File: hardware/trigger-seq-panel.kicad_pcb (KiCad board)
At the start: 2 copper layers, 89.1 x 104.6 mm, 98 parts, among them J1 OUT1, J2 OUT2, J3 RESET, J4 CLOCK_IN, J5 RUN_STOP, J6 UP_DOWN, J7 CLOCK_OUT, P3 SWITCH_PANEL, P8 JACKS_PANEL, Q6 2N3904, SW1 SW_SPDT, SW10 SW_SPDT, SW11 SW_SPDT, SW12 SW_SPDT, SW13 SW_SPDT, SW14 SW_SPDT, SW15 SW_SPDT, SW16 SW_SPDT, SW17 SW_SPDT, SW18 Run/Stop, SW19 Up/Down, SW2 SW_SPDT, SW20 RESET, SW3 SW_SPDT, SW4 SW_SPDT, SW5 SW_SPDT, SW6 SW_SPDT, SW7 SW_SPDT, SW8 SW_SPDT, SW9 SW_DPDT_x2, U2 TL072

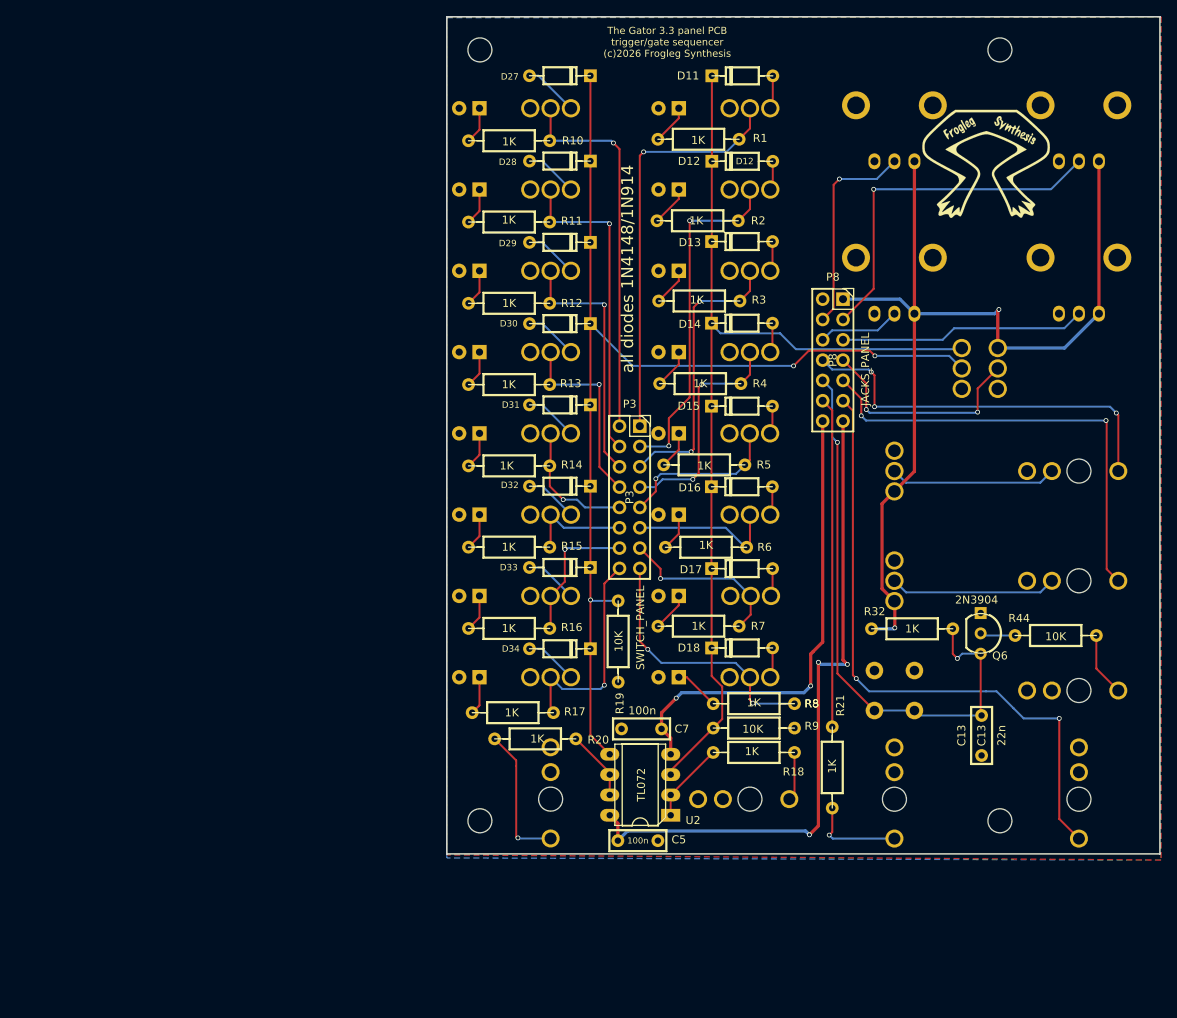
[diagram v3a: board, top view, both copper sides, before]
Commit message: update for version 3.3, slight tweaks to v3.2 which has now passed smoke test.
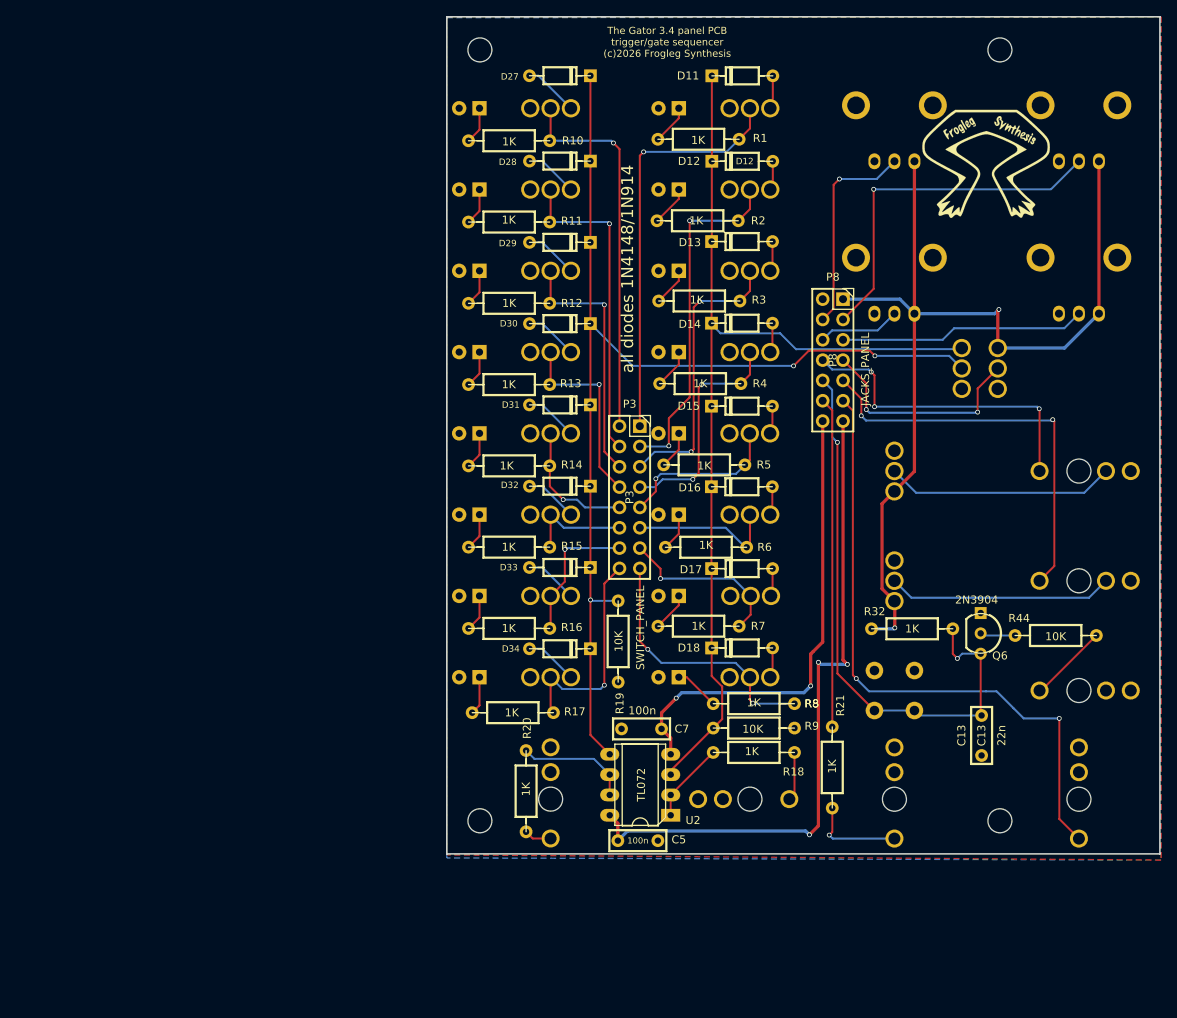
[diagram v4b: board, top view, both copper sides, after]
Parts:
- moved R20 12.3 mm to (129.0, 136.7), turned to 90 degrees
- turned J3 to -90 degrees
- turned J5 to -90 degrees
- turned J6 to -90 degrees
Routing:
- net Net-(J2-Pad1): track 17.8 -> 3.41 mm, vias 1 -> 0
- net R/S: track 49.1 -> 39.7 mm
- net Net-(J5-Pad2): track 20.9 -> 28.7 mm
- net Net-(J6-Pad2): track 20.9 -> 28.2 mm
- net U/D: track 57.1 -> 50.6 mm
- net Net-(R20-Pad2): track 8.76 -> 14.2 mm
- net Net-(J3-Pad1): track 8.01 -> 9.95 mm
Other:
- board text added: "The Gator 3.4 panel PCB trigger/gate sequencer (c)2026 Frogleg Synthesis"
- board text removed: "The Gator 3.3 panel PCB trigger/gate sequencer (c)2026 Frogleg Synthesis"

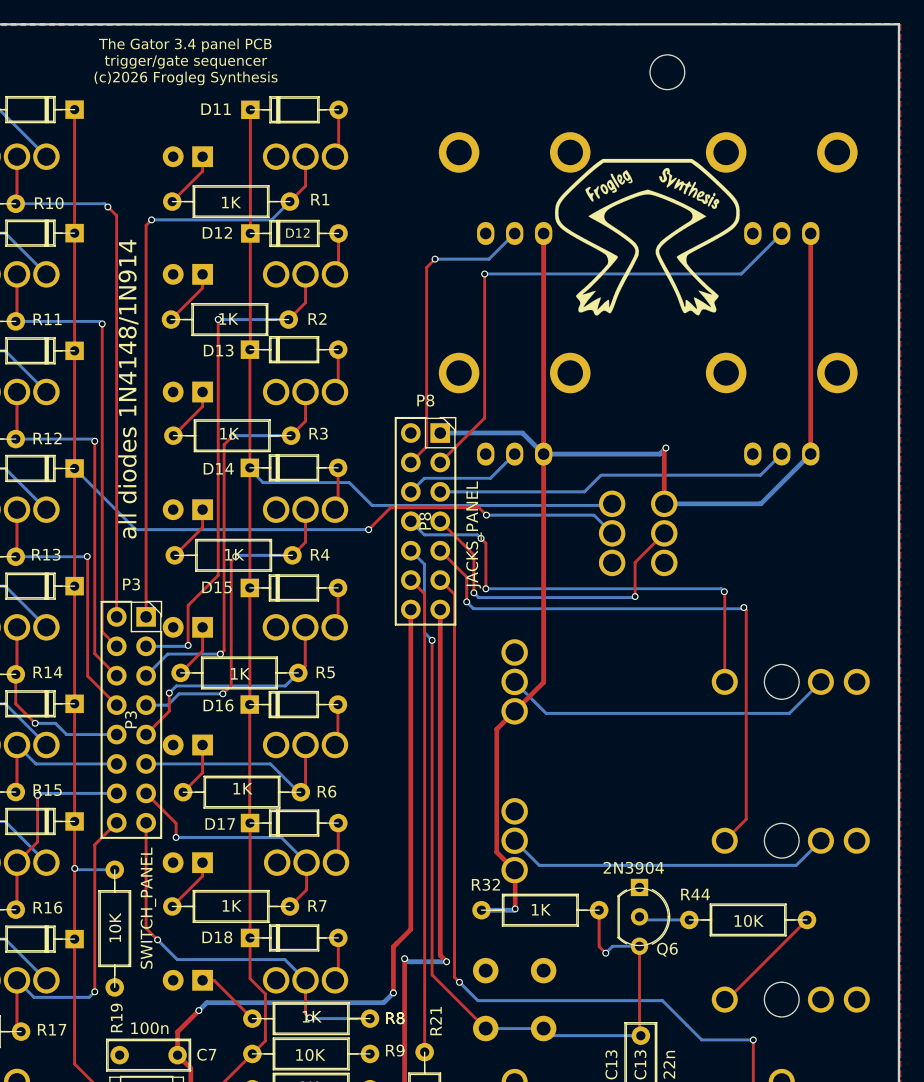
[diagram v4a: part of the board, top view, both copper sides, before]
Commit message: adjusting panel layout (increasing vertical distance of pots, compressing vertical distance of switches, centering 1x16/2x8 switch)
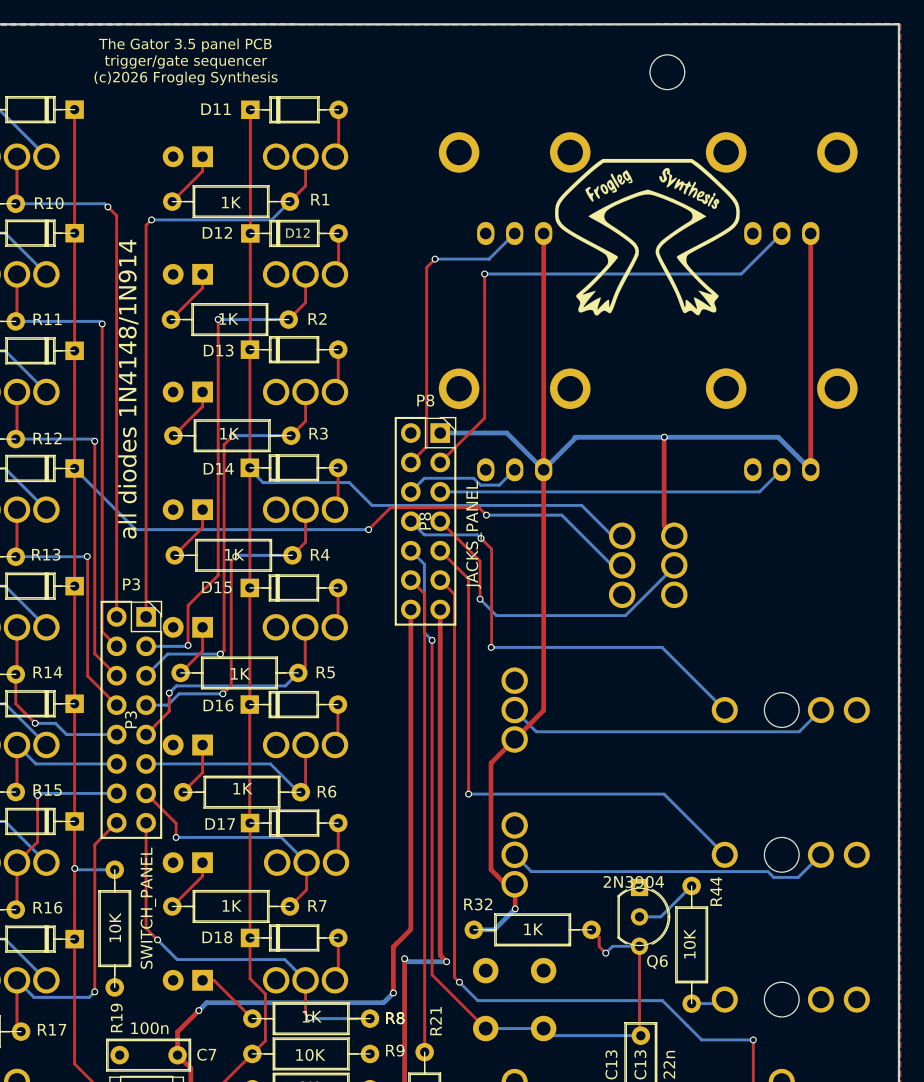
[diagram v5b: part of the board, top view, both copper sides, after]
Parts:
- moved R44 2.94 mm to (190.3, 109.3), turned to -90 degrees
- moved SW9 2.89 mm to (186.5, 81.6)
- moved J5 2.43 mm to (198.1, 94.1)
- moved SW18 2.43 mm to (175.0, 94.1)
- moved R32 1.82 mm to (171.5, 113.1)
- moved RV3 1.36 mm to (198.1, 66.3)
- moved RV4 1.36 mm to (175.0, 66.3)
- moved J6 1.22 mm to (198.1, 106.6)
- moved SW19 1.22 mm to (175.0, 106.6)
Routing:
- net +5V: track 122.4 -> 132.4 mm
- net Net-(J3-Pad1): track 9.95 -> 3.23 mm
- net U/D: track 50.6 -> 46.3 mm, vias 2 -> 1
- net Net-(D27-Pad1): track 139.6 -> 141.6 mm
- net Net-(D11-Pad1): track 123.4 -> 125.3 mm
- net reset: track 72.5 -> 71.0 mm
- net Net-(Q6-Pad2): track 4.41 -> 5.61 mm
- net R/S: track 39.7 -> 38.9 mm, vias 3 -> 2
- net Net-(J5-Pad2): track 28.7 -> 28.0 mm
- net steps: track 30.8 -> 30.3 mm
- net 2x8/1x16: track 28.0 -> 28.3 mm, vias 2 -> 1
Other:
- board text added: "The Gator 3.5 panel PCB trigger/gate sequencer (c)2026 Frogleg Synthesis"
- board text removed: "The Gator 3.4 panel PCB trigger/gate sequencer (c)2026 Frogleg Synthesis"
